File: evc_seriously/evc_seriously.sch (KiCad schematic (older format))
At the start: 23 parts

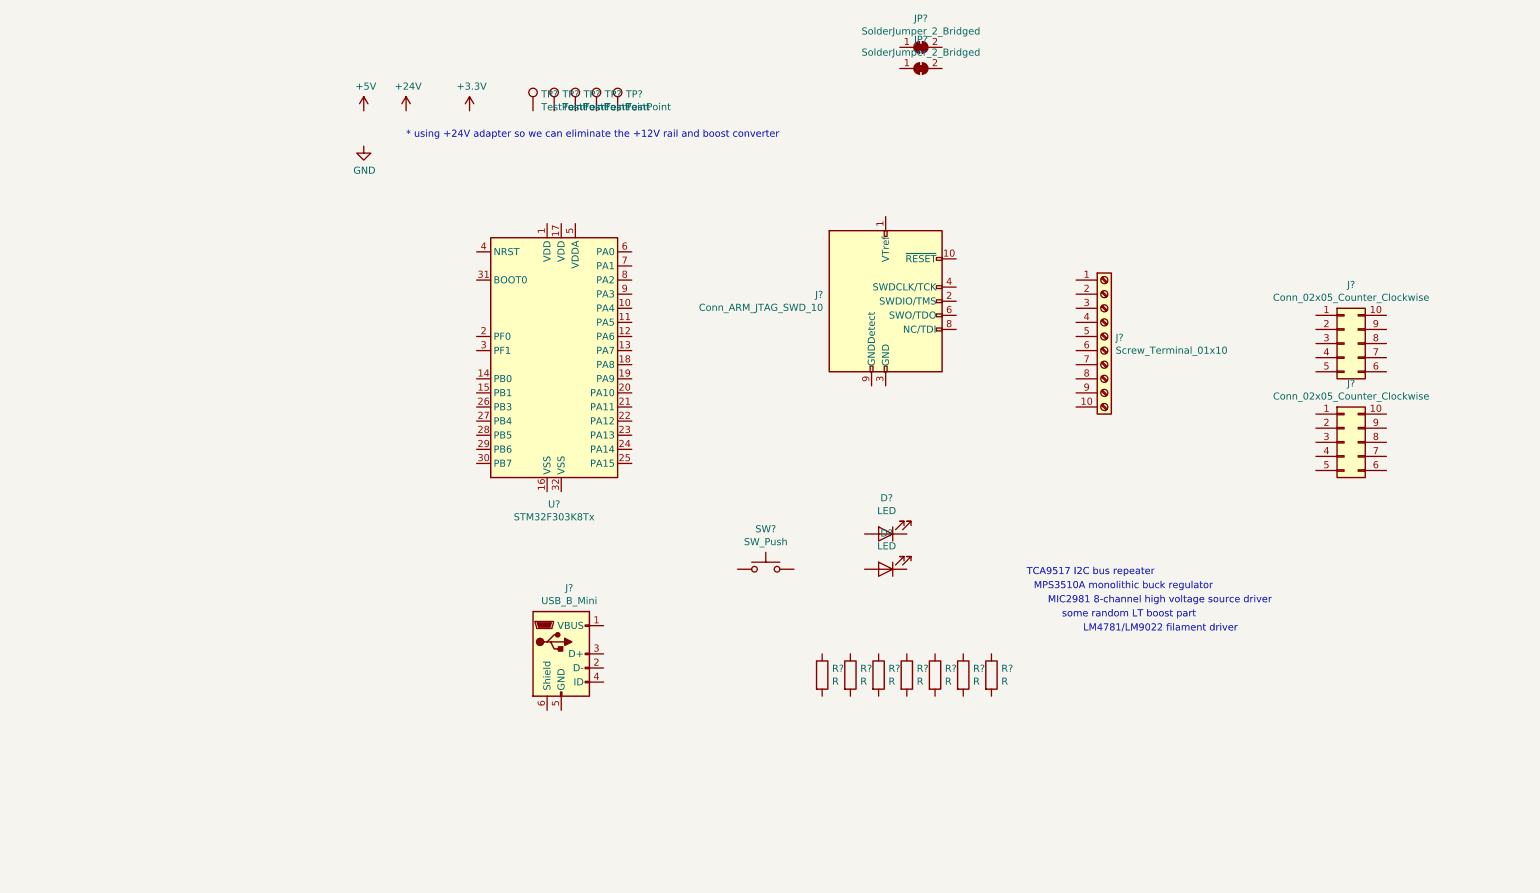
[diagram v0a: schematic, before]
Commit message: Add final footprints, begin routing board
Assign footprints to components, tune up some footprints/symbols
Add missing footprint for MPM3510A
Start placing components and routing board
HOLY CATS that buck regulator part was a pain to create a footprint for!
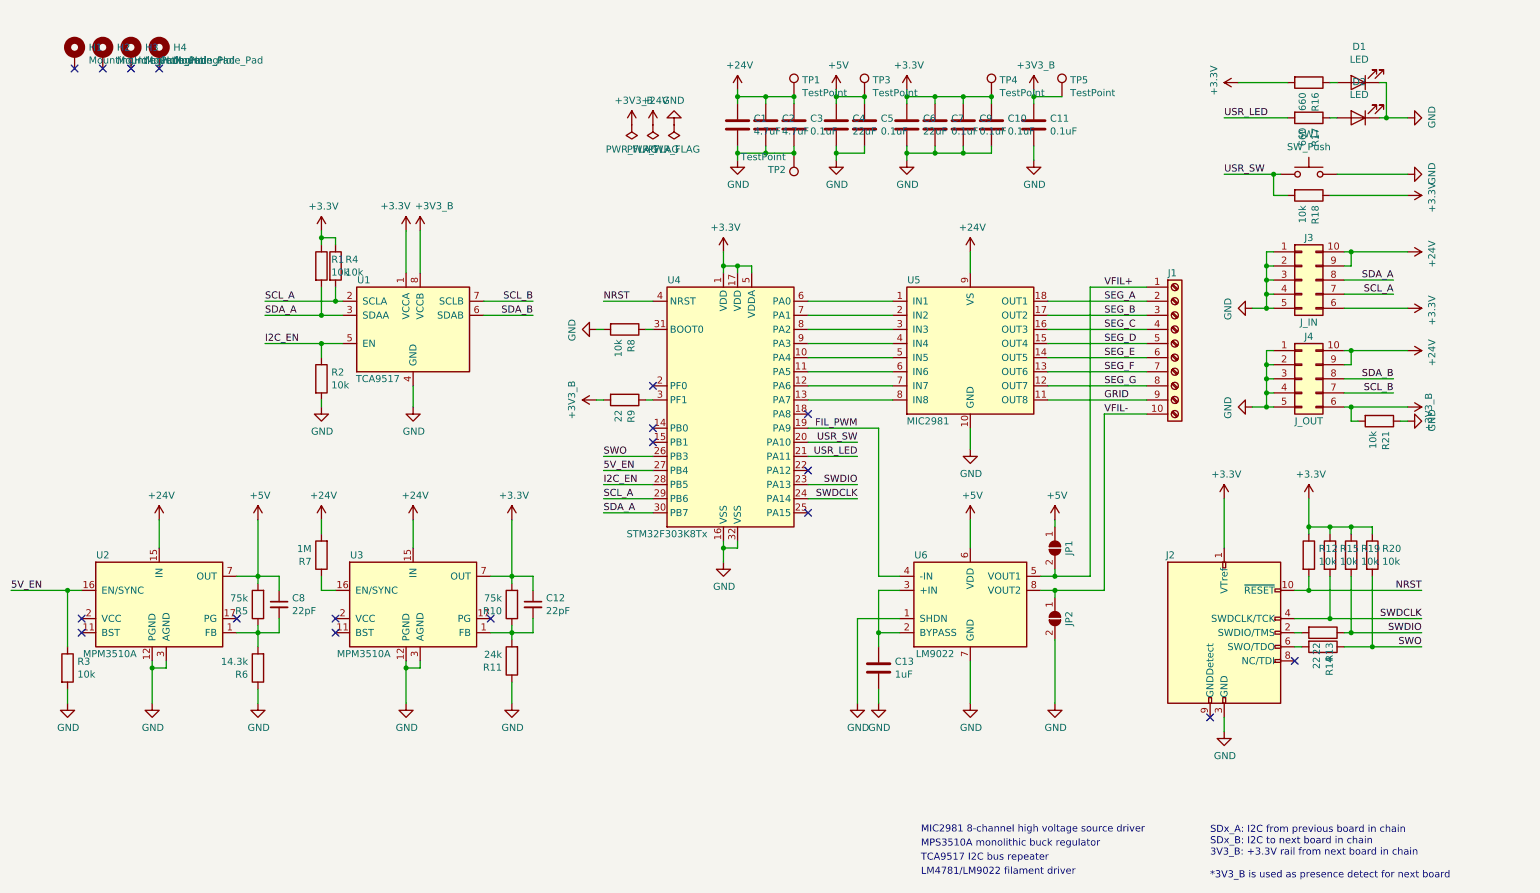
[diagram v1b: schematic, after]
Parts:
- removed J?: USB_B_Mini, symbol Connector:USB_B_Mini
- removed JP? (x2): SolderJumper_2_Bridged, symbol Jumper:SolderJumper_2_Bridged
- removed R? (x3): R, symbol Device:R
- added C1, C2: 4.7uF, Capacitor_SMD:CP_Elec_5x5.8, symbol Device:C
- added C10, C11, C3, C5, C7, C9: 0.1uF, Capacitor_SMD:C_0603_1608Metric, symbol Device:C
- added C12, C8: 22pF, Capacitor_SMD:C_0603_1608Metric, symbol Device:C_Small
- added C13: 1uF, Capacitor_SMD:C_0603_1608Metric, symbol Device:C
- added C4, C6: 22uF, Capacitor_SMD:CP_Elec_5x5.8, symbol Device:C
- added H1, H2, H3, H4: MountingHole_Pad, MountingHole:MountingHole_3.2mm_M3_Pad, symbol Mechanical:MountingHole_Pad
- added JP1, JP2: SolderJumper_2_Open, Jumper:SolderJumper-2_P1.3mm_Open_TrianglePad1.0x1.5mm, symbol Jumper:SolderJumper_2_Open
- added R1, R15, R18, R19, R2, R20, R21, R3, R4: 10k, Resistor_SMD:R_0603_1608Metric, symbol Device:R
- added R10, R5: 75k, Resistor_SMD:R_0603_1608Metric, symbol Device:R
- added R11: 24k, Resistor_SMD:R_0603_1608Metric, symbol Device:R
- added R13, R14, R9: 22, Resistor_SMD:R_0603_1608Metric, symbol Device:R
- added R6: 14.3k, Resistor_SMD:R_0603_1608Metric, symbol Device:R
- added R7: 1M, Resistor_SMD:R_0603_1608Metric, symbol Device:R
- added U1: TCA9517, Package_SO:SOIC-8_3.9x4.9mm_P1.27mm, symbol evc_seriously:TCA9517
- added U2, U3: MPM3510A, evc_seriously:QFN-19_3x5mm_P0.6mm, symbol evc_seriously:MPM3510A
- added U5: MIC2981, Package_SO:SOIC-18W_7.5x11.6mm_P1.27mm, symbol evc_seriously:MIC2981
- added U6: LM9022, Package_SO:SO-8_3.9x4.9mm_P1.27mm, symbol evc_seriously:LM9022
- D1, D2: renamed from D?; footprint (none) -> LED_SMD:LED_0805_2012Metric
- J1: renamed from J?; footprint (none) -> Connector_Phoenix_MSTB:PhoenixContact_MSTBVA_2,5_10-G_1x10_P5.00mm_Vertical
- J2: renamed from J?; footprint (none) -> Connector_PinHeader_1.27mm:PinHeader_2x05_P1.27mm_Vertical
- J3: renamed from J?; value Conn_02x05_Counter_Clockwise -> J_IN; footprint (none) -> Connector_PinHeader_2.54mm:PinHeader_2x05_P2.54mm_Vertical
- J4: renamed from J?; value Conn_02x05_Counter_Clockwise -> J_OUT; footprint (none) -> Connector_PinHeader_2.54mm:PinHeader_2x05_P2.54mm_Vertical
- R12, R8: renamed from R?; value R -> 10k; footprint (none) -> Resistor_SMD:R_0603_1608Metric
- R16, R17: renamed from R?; value R -> 660; footprint (none) -> Resistor_SMD:R_0603_1608Metric
- SW1: renamed from SW?; footprint (none) -> Button_Switch_SMD:Panasonic_EVQPUK_EVQPUB
- TP1, TP2, TP3, TP4, TP5: renamed from TP?; footprint (none) -> TestPoint:TestPoint_Pad_D1.0mm
- gave numbers to parts that had none: 1
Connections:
- net +24V: now also J3.10 (Pin_10), J3.9 (Pin_9), J4.10 (Pin_10), J4.9 (Pin_9), TP1.1, C1.2, C2.2, C3.2, R7.2, U2.15 (IN), U3.15 (IN), U5.9 (VS)
- net +3V3: now also J2.1 (VTref), J3.6 (Pin_6), R12.1, R16.2, TP4.1, U4.1 (VDD), U4.17 (VDD), U4.5 (VDDA), C10.2, C12.1, C6.2, C7.2, C9.2, R1.1, R10.2, R15.1, R18.1, R19.1, R20.1, R4.1, U1.1 (VCCA), U3.7 (OUT), U3.8 (OUT), U3.9 (OUT)
- net +5V: now also TP3.1, C4.2, C5.2, C8.1, JP1.1 (A), R5.2, U2.7 (OUT), U2.8 (OUT), U2.9 (OUT), U6.6 (VDD)
- net GND: now also D1.1 (K), D2.1 (K), J2.3 (GND), J2.5 (GND), J3.1 (Pin_1), J3.2 (Pin_2), J3.3 (Pin_3), J3.4 (Pin_4), J3.5 (Pin_5), J4.1 (Pin_1), J4.2 (Pin_2), J4.3 (Pin_3), J4.4 (Pin_4), J4.5 (Pin_5), R8.2, SW1.2, TP2.1, U4.16 (VSS), U4.32 (VSS), C1.1, C10.1, C11.1, C13.1, C2.1, C3.1, C4.1, C5.1, C6.1, C7.1, C9.1, JP2.2 (B), R11.1, R2.2, R21.1, R3.2, R6.1, U1.4 (GND), U2.12 (PGND), U2.13 (PGND), U2.3 (AGND), U3.12 (PGND), U3.13 (PGND), U3.3 (AGND), U5.10 (GND), U6.1 (SHDN), U6.7 (GND)
- net at U4.10 (PA4): now also U5.5 (IN5)
- net at U4.11 (PA5): now also U5.6 (IN6)
- net at U4.12 (PA6): now also U5.7 (IN7)
- net at U4.13 (PA7): now also U5.8 (IN8)
- net FIL_PWM: now reaches U4.19 (PA9)
- net FIL_PWM: now also U6.4 (-IN)
- net USR_SW: now reaches U4.20 (PA10)
- net USR_SW: now also SW1.1, R18.2
- net USR_LED: now reaches U4.21 (PA11)
- net USR_LED: now also R17.2
- net SWDIO: now reaches U4.23 (PA13)
- net SWDIO: now also R13.1, R19.2
- net SWDCLK: now reaches U4.24 (PA14)
- net SWDCLK: now also J2.4 (SWDCLK/TCK), R15.2
- net SWO: now reaches U4.26 (PB3)
- net SWO: now also R14.1, R20.2
- net 5V_EN: now reaches U4.27 (PB4)
- net 5V_EN: now also R3.1, U2.16 (EN/SYNC)
- net I2C_EN: now reaches U4.28 (PB5)
- net I2C_EN: now also R2.1, U1.5 (EN)
- net SCL_A: now reaches U4.29 (PB6)
- net SCL_A: now also J3.7 (Pin_7), R4.2, U1.2 (SCLA)
- net at U4.3 (PF1): now also R9.1
- net SDA_A: now reaches U4.30 (PB7)
- net SDA_A: now also J3.8 (Pin_8), R1.2, U1.3 (SDAA)
- net at U4.31 (BOOT0): now also R8.1
- net NRST: now reaches U4.4 (NRST)
- net NRST: now also J2.10 (~RESET~), R12.2
- net at U4.6 (PA0): now also U5.1 (IN1)
- net at U4.7 (PA1): now also U5.2 (IN2)
- net at U4.8 (PA2): now also U5.3 (IN3)
- net at U4.9 (PA3): now also U5.4 (IN4)
- net VFIL+: now reaches J1.1 (Pin_1)
- net VFIL+: now also JP1.2 (B), U6.5 (VOUT1)
- net VFIL-: now reaches J1.10 (Pin_10)
- net VFIL-: now also JP2.1 (A), U6.8 (VOUT2)
- net SEG_A: now reaches J1.2 (Pin_2)
- net SEG_A: now also U5.18 (OUT1)
- net SEG_B: now reaches J1.3 (Pin_3)
- net SEG_B: now also U5.17 (OUT2)
- net SEG_C: now reaches J1.4 (Pin_4)
- net SEG_C: now also U5.16 (OUT3)
- net SEG_D: now reaches J1.5 (Pin_5)
- net SEG_D: now also U5.15 (OUT4)
- net SEG_E: now reaches J1.6 (Pin_6)
- net SEG_E: now also U5.14 (OUT5)
- net SEG_F: now reaches J1.7 (Pin_7)
- net SEG_F: now also U5.13 (OUT6)
- net SEG_G: now reaches J1.8 (Pin_8)
- net SEG_G: now also U5.12 (OUT7)
- net GRID: now reaches J1.9 (Pin_9)
- net GRID: now also U5.11 (OUT8)
- net at J2.2 (SWDIO/TMS): now also R13.2
- net at J2.6 (SWO/TDO): now also R14.2
- net at D1.2 (A): now also R16.1
- net at D2.2 (A): now also R17.1
- net +3V3_B: now reaches J4.6 (Pin_6)
- net +3V3_B: now also TP5.1, C11.2, R21.2, R9.2, U1.8 (VCCB)
- net SCL_B: now reaches J4.7 (Pin_7)
- net SCL_B: now also U1.7 (SCLB)
- net SDA_B: now reaches J4.8 (Pin_8)
- net SDA_B: now also U1.6 (SDAB)
- new net: C13.2, U6.2 (BYPASS), U6.3 (+IN)
- new net: C8.2, R5.1, R6.2, U2.1 (FB)
- new net: U2.4 (SW), U2.5 (SW), U2.6 (SW)
- new net: C12.2, R10.1, R11.2, U3.1 (FB)
- new net: R7.1, U3.16 (EN/SYNC)
- new net: U3.4 (SW), U3.5 (SW), U3.6 (SW)
- no-connect marks 0 -> 18
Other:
- note added: "SDx_A: I2C from previous board in chain\nSDx_B: I2C to next board in chain\n3V3_B: +3.3V rail from next board in chain\n\n*3V3_B is used as presence detect for next board"
- note removed: "* using +24V adapter so we can eliminate the +12V rail and boost converter"
- note removed: "some random LT boost part"
- moved on the sheet: D1, D2, J1, J2, J3, J4, R12, R16, R17, R8, SW1, TP1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
